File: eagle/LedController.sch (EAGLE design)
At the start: 32 parts, among them IC1 MCP601R, IC2 MEGA8-P, IC3 7805, Q1 16MHz, Q2 FDS8884, Q3 FDS8884, Q4 FDS8884, Q5 FDS8884, X1 2510-, X2 MKDSN1,5/4-5,08

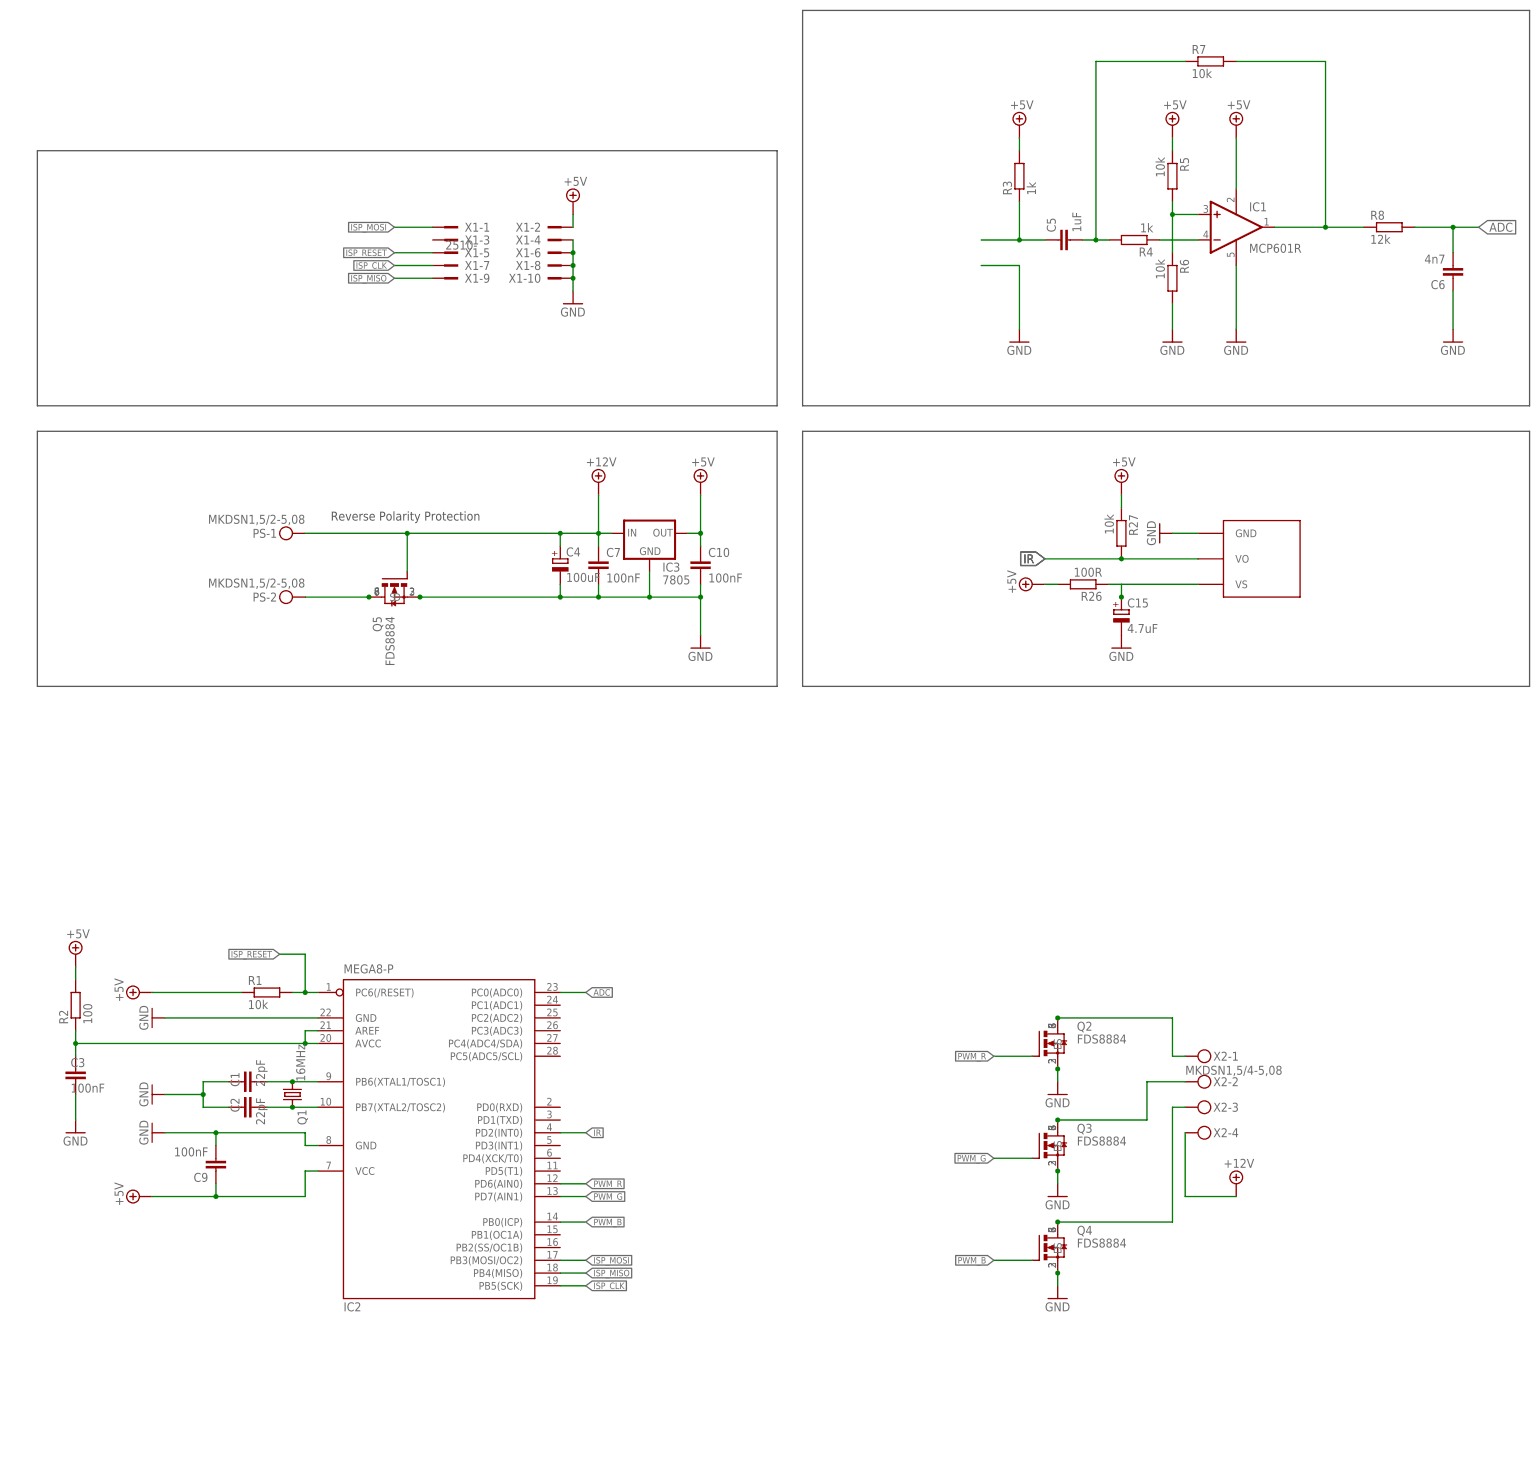
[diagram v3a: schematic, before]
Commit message: Replace atmega8 (DIP) with atmega328 (TQFP), start of redesign
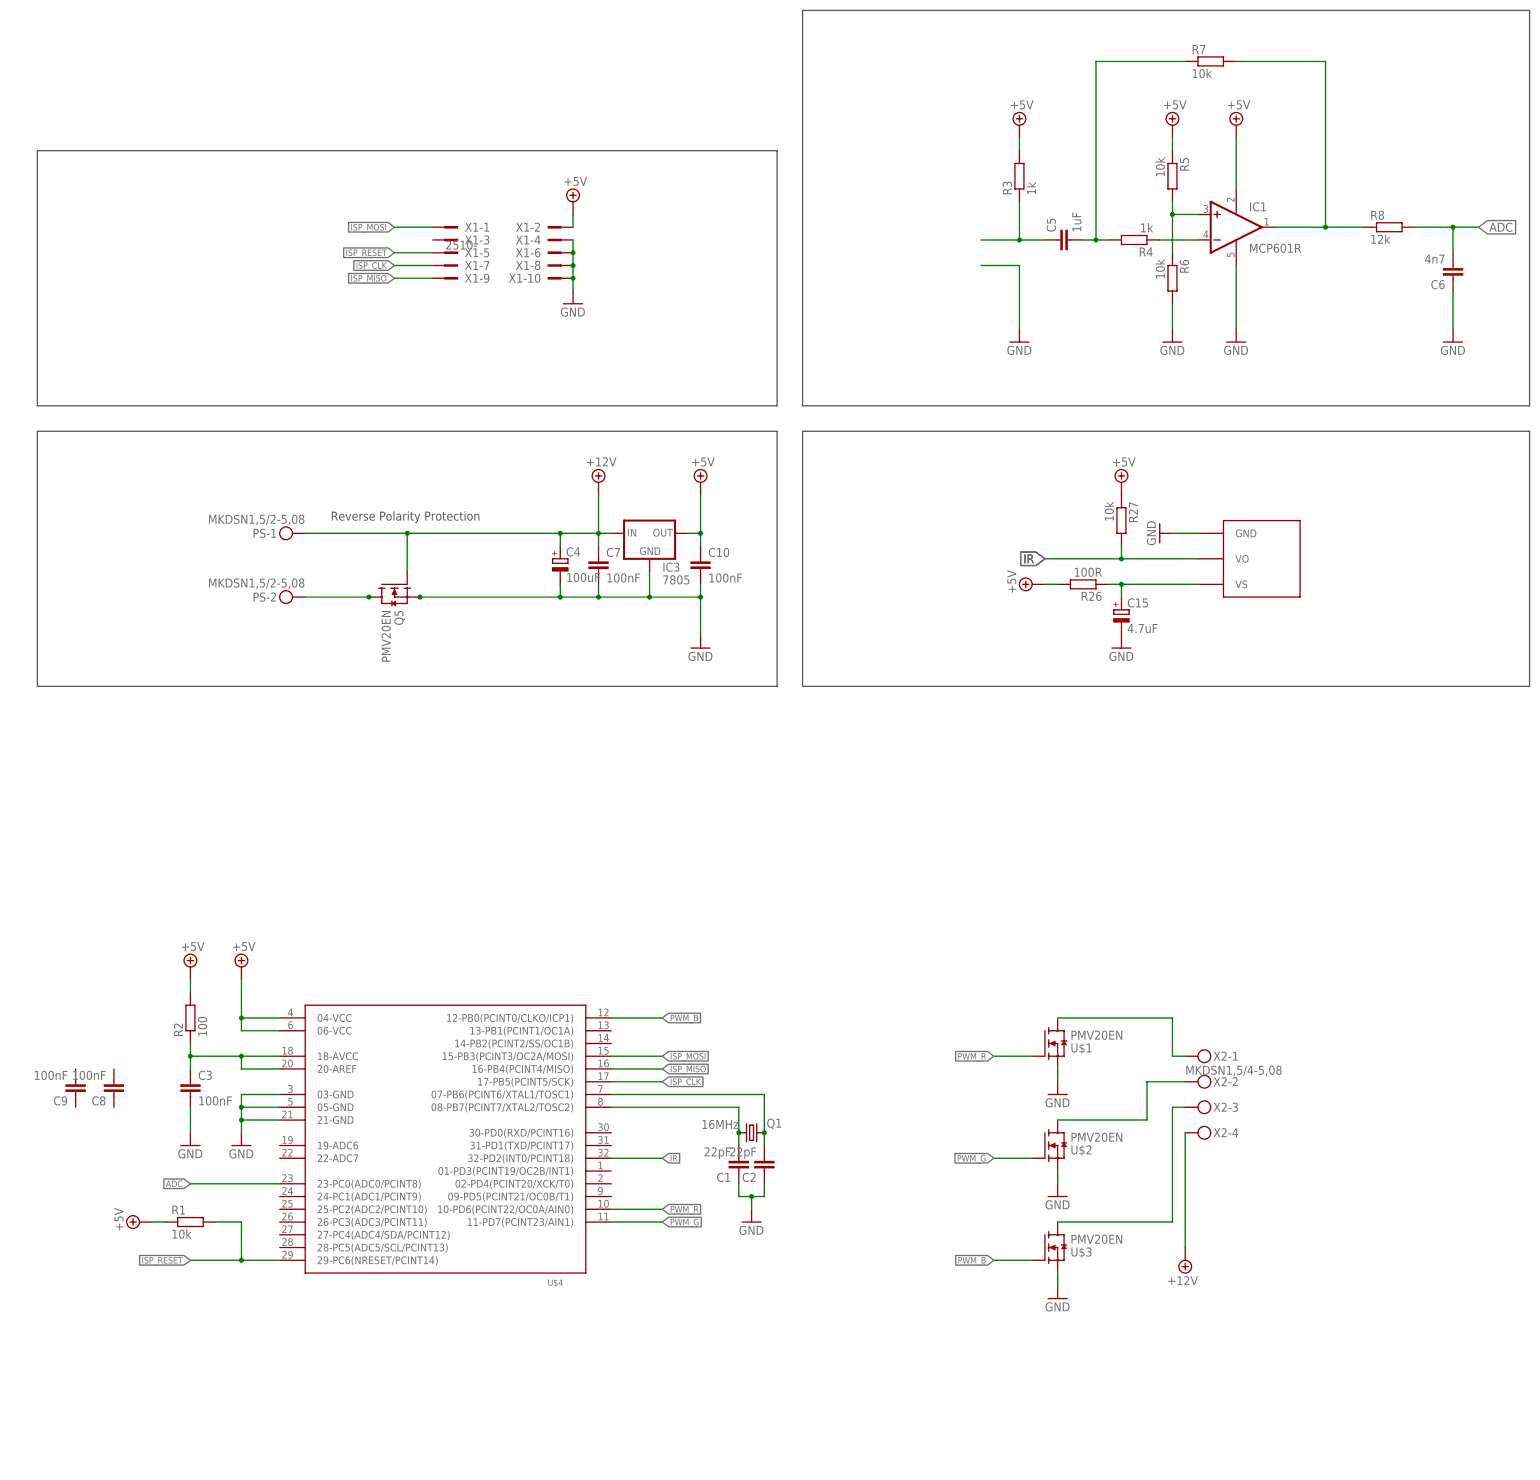
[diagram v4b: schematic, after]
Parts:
- removed IC2: MEGA8-P, atmel:MEGA8-P
- removed Q2, Q3, Q4: FDS8884, FDS8884:FDS8884
- added C8: 100nF, rcl:C-EUC0805
- added U$1, U$2, U$3: PMV20EN, LedController:PMV20EN
- added U$4: ATMEGA328, LedController:ATMEGA328
- C1, C2, C3: device rcl:C-EU025-025X050 -> rcl:C-EUC0805
- C10, C5, C6, C7, C9: device rcl:C-EU025-024X044 -> rcl:C-EUC0805
- Q5: value FDS8884 -> PMV20EN; device FDS8884:FDS8884 -> LedController:PMV20EN
- R2, R4, R5, R6, R7, R8: device rcl:R-EU_0207/2V -> rcl:R-EU_R0805
- R26, R27: device rcl:R-EU_0207/10 -> rcl:R-EU_R0805
- R3: device rcl:R-EU_0207/2V -> rcl:R-EU_M0805
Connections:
- removed net N$2: C1.2, IC2.PB6(XTAL1/TOSC1), Q1.2
- new net N$13: C1.2, Q1.2, U$4.08-PB7(PCINT7/XTAL2/TOSC2)
- net +5V: now also U$4.04-VCC, U$4.06-VCC; no longer C9.1, IC2.VCC@1
- net ADC: now also U$4.23-PC0(ADC0/PCINT8); no longer IC2.PC0(ADC0)
- net GND: now also U$1.S, U$2.S, U$3.S, U$4.03-GND, U$4.05-GND, U$4.21-GND; no longer C9.2, IC2.GND, IC2.GND@1, Q2.S, Q2.S@1, Q2.S@2, Q3.S, Q3.S@1, Q3.S@2, Q4.S, Q4.S@1, Q4.S@2, Q5.S@1, Q5.S@2
- net IR: now also U$4.32-PD2(INT0/PCINT18); no longer IC2.PD2(INT0)
- net ISP_CLK: now also U$4.17-PB5(PCINT5/SCK); no longer IC2.PB5(SCK)
- net ISP_MISO: now also U$4.16-PB4(PCINT4/MISO); no longer IC2.PB4(MISO)
- net ISP_MOSI: now also U$4.15-PB3(PCINT3/OC2A/MOSI); no longer IC2.PB3(MOSI/OC2)
- net ISP_RESET: now also U$4.29-PC6(NRESET/PCINT14); no longer IC2.PC6(/RESET)
- net N$3: now also U$4.07-PB6(PCINT6/XTAL1/TOSC1); no longer IC2.PB7(XTAL2/TOSC2)
- net N$4: now also U$1.D; no longer Q2.D, Q2.D@1, Q2.D@2, Q2.D@3
- net N$5: now also U$2.D; no longer Q3.D, Q3.D@1, Q3.D@2, Q3.D@3
- net N$6: now also U$3.D; no longer Q4.D, Q4.D@1, Q4.D@2, Q4.D@3
- net N$7: now also U$4.18-AVCC, U$4.20-AREF; no longer IC2.AREF, IC2.AVCC
- net N$8: no longer Q5.D@1, Q5.D@2, Q5.D@3
- net PWM_B: now also U$3.G, U$4.12-PB0(PCINT0/CLKO/ICP1); no longer IC2.PB0(ICP), Q4.G
- net PWM_G: now also U$2.G, U$4.11-PD7(PCINT23/AIN1); no longer IC2.PD7(AIN1), Q3.G
- net PWM_R: now also U$1.G, U$4.10-PD6(PCINT22/OC0A/AIN0); no longer IC2.PD6(AIN0), Q2.G
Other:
- moved on the sheet: C1, C2, C3, C9, Q1, R1, R2, R27

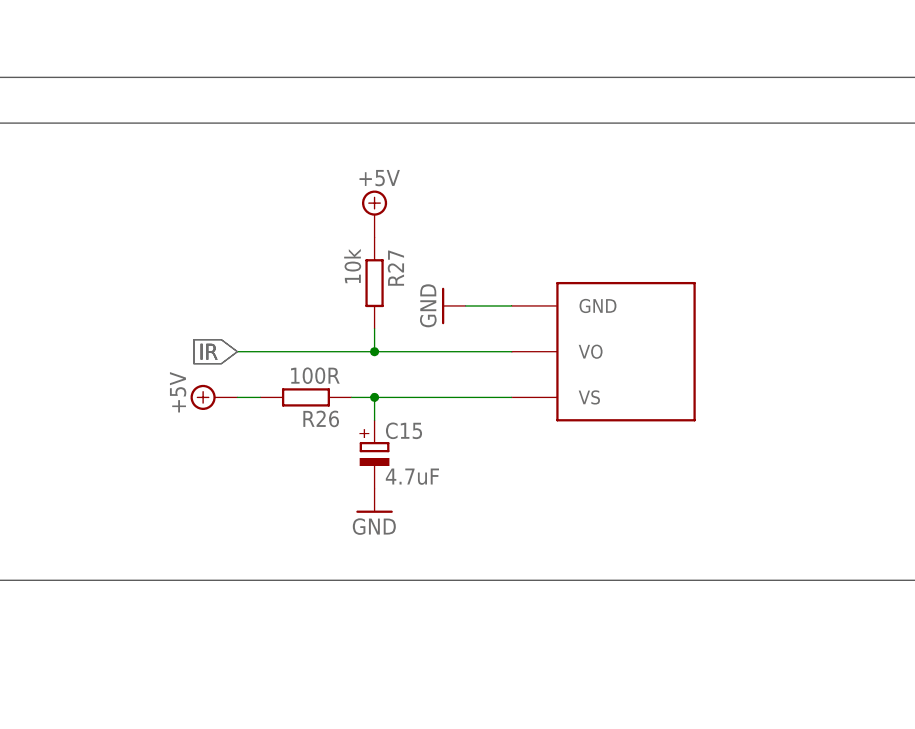
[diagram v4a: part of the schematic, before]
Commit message: Change IR Receiver module to SMD variant
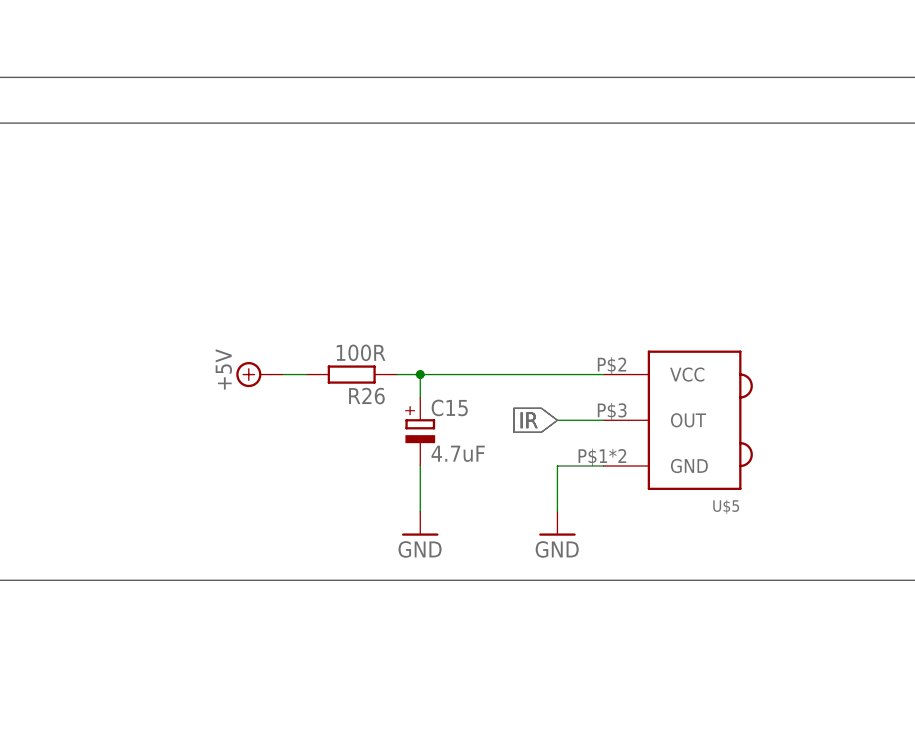
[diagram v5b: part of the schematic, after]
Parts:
- removed R27: 10k, rcl:R-EU_R0805
- removed TSOP: TSOP, TSOP1736:TSOP
- added U$5: TSOP75236, LedController:TSOP75236
- R1: device rcl:R-EU_0207/2V -> rcl:R-EU_R0805
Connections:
- net +5V: no longer R27.1
- net GND: now also U$5.GND; no longer TSOP.GND
- net IR: now also U$5.OUT; no longer R27.2, TSOP.VO
- net N$63: now also U$5.VCC; no longer TSOP.VS
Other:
- moved on the sheet: C15, R26

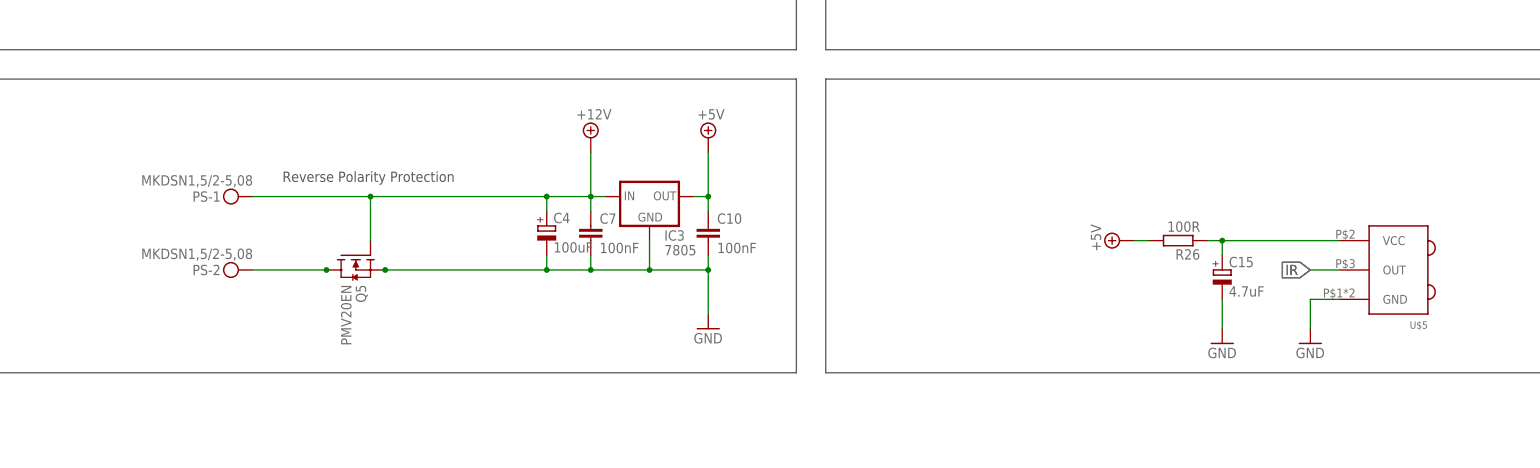
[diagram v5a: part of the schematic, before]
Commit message: Change voltage regulator to DPAK variant
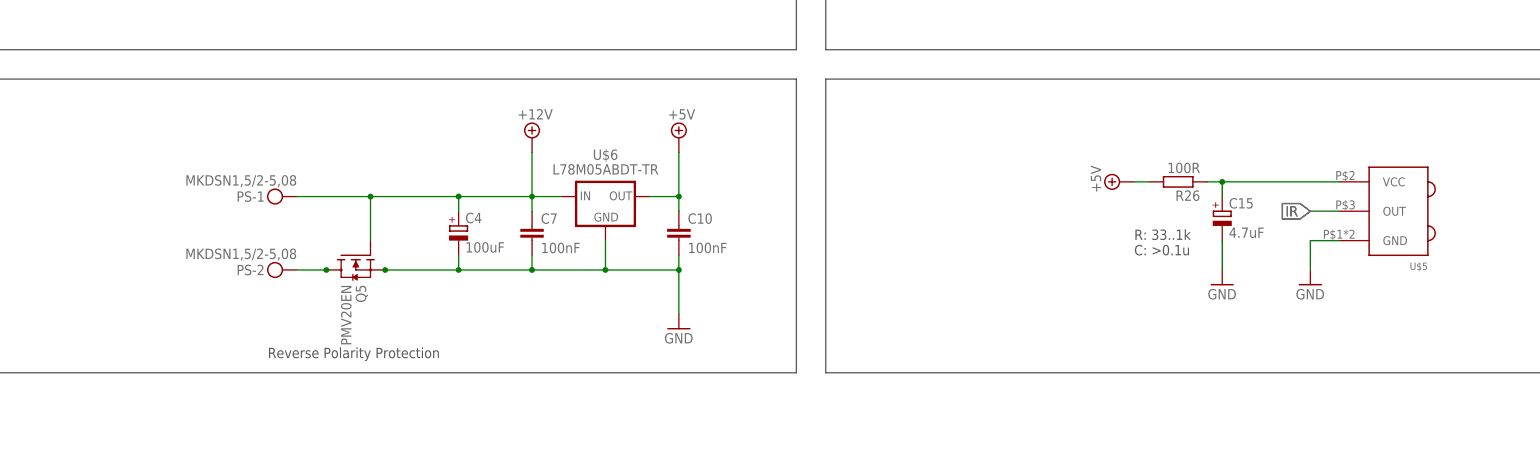
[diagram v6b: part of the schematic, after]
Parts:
- removed IC3: 7805, v-reg:78XXS
- added U$6: L78M05ABDT-TR, LedController:L78M05ABDT-TR
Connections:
- net +12V: now also U$6.IN; no longer IC3.IN
- net +5V: now also U$6.OUT; no longer IC3.OUT
- net GND: now also U$6.GND; no longer IC3.GND
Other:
- note added: "R: 33..1k C: >0.1u"
- moved on the sheet: C10, C15, C4, C7, PS-1, PS-2, R26, U$5
